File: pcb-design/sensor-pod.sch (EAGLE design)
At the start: 21 parts, among them X1 PH_SENSOR, X10 I2C_5V, X11 3.3V, X12 3.3V, X15 MB-LEFT, X16 MB-RIGHT, X3 TURBIDITY, X4 5V, X5 TEMPERATURE, X6 MOTOR_1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

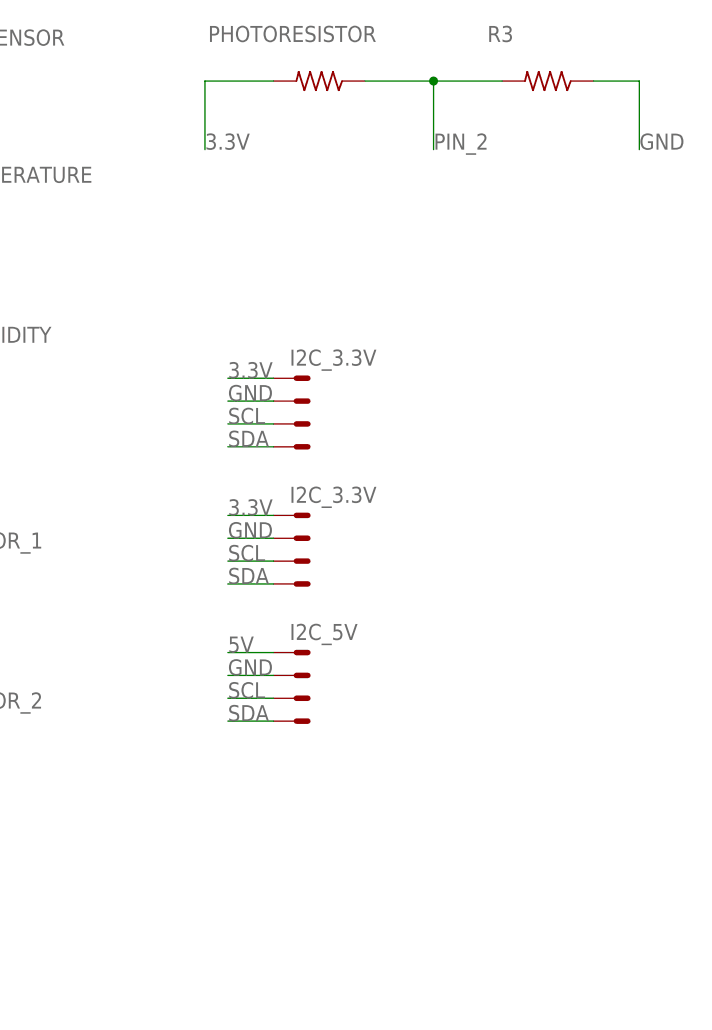
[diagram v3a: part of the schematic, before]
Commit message: pcd-design: Decreased distance between components and microbit interface. Increased PCB size.
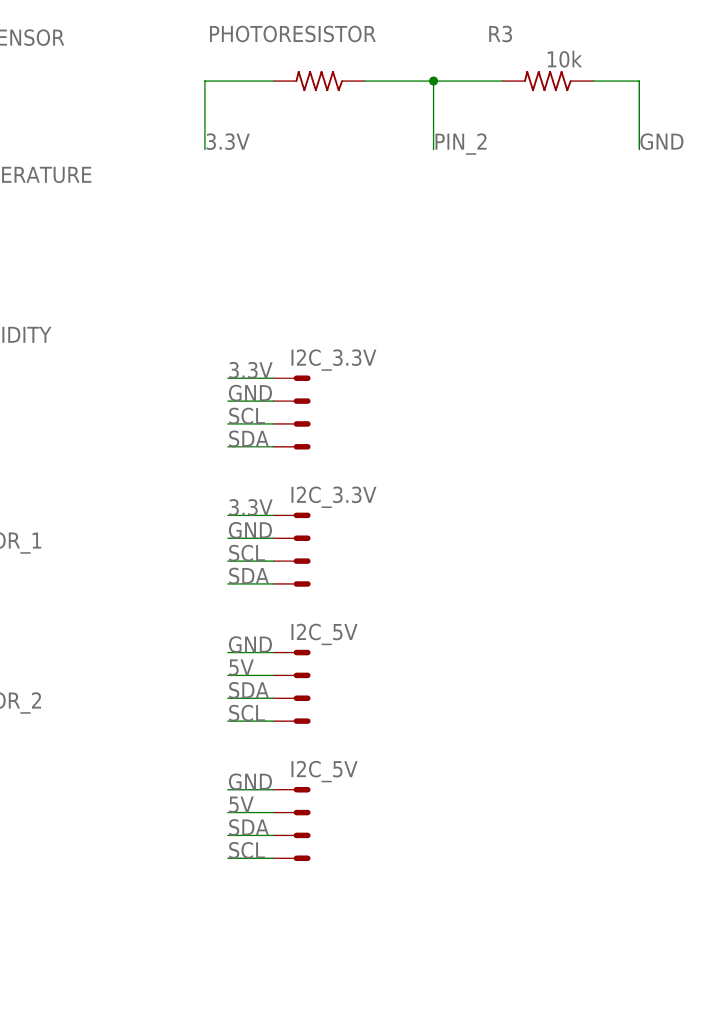
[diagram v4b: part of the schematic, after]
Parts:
- added X2: I2C_5V, con-molex:22-23-2041
- R3: value (none) -> 10k
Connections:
- net 5V: now also X10-2.S, X2-2.S; no longer X10-1.S
- net GND: now also X10-1.S, X2-1.S; no longer X10-2.S
- net SCL: now also X10-4.S, X2-4.S; no longer X10-3.S
- net SDA: now also X10-3.S, X2-3.S; no longer X10-4.S
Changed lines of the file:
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@@
 <part name="R1" library="rcl" library_urn="urn:adsk.eagle:library:334" deviceset="R-US_" device="0204/7" package3d_urn="urn:adsk.eagle:package:23498/2" value="4.7k"/>
 <part name="PHOTORESISTOR" library="rcl" library_urn="urn:adsk.eagle:library:334" deviceset="R-US_" device="0204/7" package3d_urn="urn:adsk.eagle:package:23498/2"/>
-<part name="R3" library="rcl" library_urn="urn:adsk.eagle:library:334" deviceset="R-US_" device="0204/7" package3d_urn="urn:adsk.eagle:package:23498/2"/>
+<part name="R3" library="rcl" library_urn="urn:adsk.eagle:library:334" deviceset="R-US_" device="0204/7" package3d_urn="urn:adsk.eagle:package:23498/2" value="10k"/>
 <part name="D1" library="led" library_urn="urn:adsk.eagle:library:259" deviceset="SFH482" device="" package3d_urn="urn:adsk.eagle:package:15795/1" value="5V_LED"/>
 <part name="D2" library="led" library_urn="urn:adsk.eagle:library:259" deviceset="SFH482" device="" package3d_urn="urn:adsk.eagle:package:15795/1" value="3.3V_LED"/>
 <part name="R2" library="rcl" library_urn="urn:adsk.eagle:library:334" deviceset="R-US_" device="0204/7" package3d_urn="urn:adsk.eagle:package:23498/2"/>
 <part name="R4" library="rcl" library_urn="urn:adsk.eagle:library:334" deviceset="R-US_" device="0204/7" package3d_urn="urn:adsk.eagle:package:23498/2"/>
+<part name="X2" library="con-molex" library_urn="urn:adsk.eagle:library:165" deviceset="22-23-2041" device="" package3d_urn="urn:adsk.eagle:package:8078635/1" value="I2C_5V"/>
 </parts>
 <sheets>
@@
 <attribute name="VALUE" x="62.23" y="-4.318" size="1.778" layer="96" rot="R180"/>
 </instance>
+<instance part="X2" gate="-1" x="187.96" y="-27.94" smashed="yes">
+<attribute name="VALUE" x="187.198" y="-26.543" size="1.778" layer="96"/>
+</instance>
+<instance part="X2" gate="-2" x="187.96" y="-30.48" smashed="yes"/>
+<instance part="X2" gate="-3" x="187.96" y="-33.02" smashed="yes"/>
+<instance part="X2" gate="-4" x="187.96" y="-35.56" smashed="yes"/>
 </instances>
 <busses>
@@
 </segment>
 <segment>
+<pinref part="X16" gate="-4" pin="S"/>
+<wire x1="73.66" y1="40.64" x2="66.04" y2="40.64" width="0.1524" layer="91"/>
+<label x="66.04" y="40.64" size="1.778" layer="95"/>
+</segment>
+<segment>
+<pinref part="X10" gate="-4" pin="S"/>
+<wire x1="185.42" y1="-20.32" x2="180.34" y2="-20.32" width="0.1524" layer="91"/>
+<label x="180.34" y="-20.32" size="1.778" layer="95"/>
+</segment>
+<segment>
+<pinref part="X2" gate="-4" pin="S"/>
+<wire x1="185.42" y1="-35.56" x2="180.34" y2="-35.56" width="0.1524" layer="91"/>
+<label x="180.34" y="-35.56" size="1.778" layer="95"/>
+</segment>
+</net>
+<net name="SDA" class="0">
+<segment>
+<pinref part="X8" gate="-4" pin="S"/>
+<wire x1="185.42" y1="10.16" x2="180.34" y2="10.16" width="0.1524" layer="91"/>
+<label x="180.34" y="10.16" size="1.778" layer="95"/>
+</segment>
+<segment>
+<pinref part="X9" gate="-4" pin="S"/>
+<wire x1="185.42" y1="-5.08" x2="180.34" y2="-5.08" width="0.1524" layer="91"/>
+<label x="180.34" y="-5.08" size="1.778" layer="95"/>
+</segment>
+<segment>
+<pinref part="X16" gate="-3" pin="S"/>
+<wire x1="73.66" y1="43.18" x2="66.04" y2="43.18" width="0.1524" layer="91"/>
+<label x="66.04" y="43.18" size="1.778" layer="95"/>
+</segment>
+<segment>
 <pinref part="X10" gate="-3" pin="S"/>
 <wire x1="185.42" y1="-17.78" x2="180.34" y2="-17.78" width="0.1524" layer="91"/>
@@
 </segment>
 <segment>
-<pinref part="X16" gate="-4" pin="S"/>
-<wire x1="73.66" y1="40.64" x2="66.04" y2="40.64" width="0.1524" layer="91"/>
-<label x="66.04" y="40.64" size="1.778" layer="95"/>
-</segment>
-</net>
-<net name="SDA" class="0">
-<segment>
-<pinref part="X8" gate="-4" pin="S"/>
-<wire x1="185.42" y1="10.16" x2="180.34" y2="10.16" width="0.1524" layer="91"/>
-<label x="180.34" y="10.16" size="1.778" layer="95"/>
-</segment>
-<segment>
-<pinref part="X9" gate="-4" pin="S"/>
-<wire x1="185.42" y1="-5.08" x2="180.34" y2="-5.08" width="0.1524" layer="91"/>
-<label x="180.34" y="-5.08" size="1.778" layer="95"/>
-</segment>
-<segment>
-<pinref part="X10" gate="-4" pin="S"/>
-<wire x1="185.42" y1="-20.32" x2="180.34" y2="-20.32" width="0.1524" layer="91"/>
-<label x="180.34" y="-20.32" size="1.778" layer="95"/>
-</segment>
-<segment>
-<pinref part="X16" gate="-3" pin="S"/>
-<wire x1="73.66" y1="43.18" x2="66.04" y2="43.18" width="0.1524" layer="91"/>
-<label x="66.04" y="43.18" size="1.778" layer="95"/>
+<pinref part="X2" gate="-3" pin="S"/>
+<wire x1="185.42" y1="-33.02" x2="180.34" y2="-33.02" width="0.1524" layer="91"/>
+<label x="180.34" y="-33.02" size="1.778" layer="95"/>
 </segment>
 </net>
@@
 <wire x1="68.58" y1="-53.34" x2="63.5" y2="-53.34" width="0.1524" layer="91"/>
 <label x="63.5" y="-53.34" size="1.778" layer="95"/>
-</segment>
-<segment>
-<pinref part="X10" gate="-1" pin="S"/>
-<wire x1="185.42" y1="-12.7" x2="180.34" y2="-12.7" width="0.1524" layer="91"/>
-<label x="180.34" y="-12.7" size="1.778" layer="95"/>
 </segment>
 <segment>
@@
 <label x="33.02" y="-7.62" size="1.778" layer="95"/>
 </segment>
+<segment>
+<pinref part="X10" gate="-2" pin="S"/>
+<wire x1="185.42" y1="-15.24" x2="180.34" y2="-15.24" width="0.1524" layer="91"/>
+<label x="180.34" y="-15.24" size="1.778" layer="95"/>
+</segment>
+<segment>
+<pinref part="X2" gate="-2" pin="S"/>
+<wire x1="185.42" y1="-30.48" x2="180.34" y2="-30.48" width="0.1524" layer="91"/>
+<label x="180.34" y="-30.48" size="1.778" layer="95"/>
+</segment>
 </net>
 <net name="GND" class="0">
@@
 <wire x1="185.42" y1="0" x2="180.34" y2="0" width="0.1524" layer="91"/>
 <label x="180.34" y="0" size="1.778" layer="95"/>
-</segment>
-<segment>
-<pinref part="X10" gate="-2" pin="S"/>
-<wire x1="185.42" y1="-15.24" x2="180.34" y2="-15.24" width="0.1524" layer="91"/>
-<label x="180.34" y="-15.24" size="1.778" layer="95"/>
 </segment>
 <segment>
@@
 <label x="73.66" y="-30.48" size="1.778" layer="95"/>
 </segment>
+<segment>
+<pinref part="X10" gate="-1" pin="S"/>
+<wire x1="185.42" y1="-12.7" x2="180.34" y2="-12.7" width="0.1524" layer="91"/>
+<label x="180.34" y="-12.7" size="1.778" layer="95"/>
+</segment>
+<segment>
+<pinref part="X2" gate="-1" pin="S"/>
+<wire x1="185.42" y1="-27.94" x2="180.34" y2="-27.94" width="0.1524" layer="91"/>
+<label x="180.34" y="-27.94" size="1.778" layer="95"/>
+</segment>
 </net>
